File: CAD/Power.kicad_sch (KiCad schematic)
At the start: 84 parts, among them U10 AOZ1284, U18 AP7330-W5-7, U24 LM70860RRXR, U4 AP7361C-33E-13

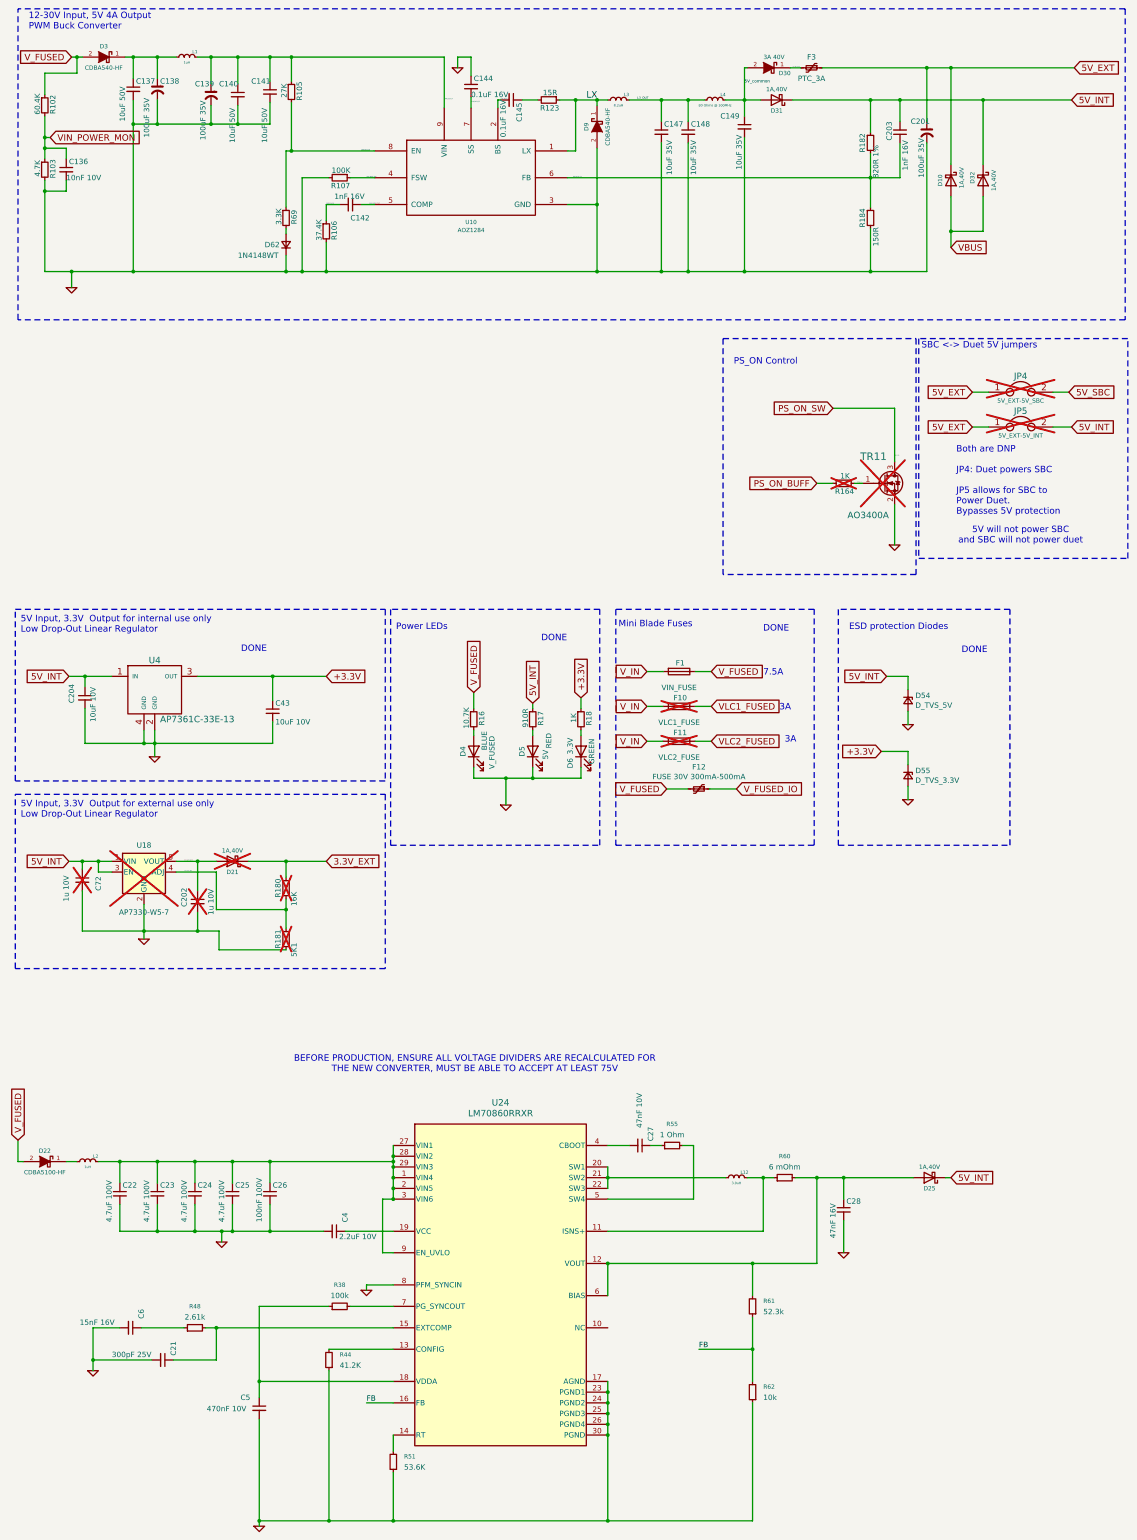
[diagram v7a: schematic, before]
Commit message: Schematic 90%
Still need VIN_POWER_MON and the voltage divider for it, I need to ask robert what voltages are input through there
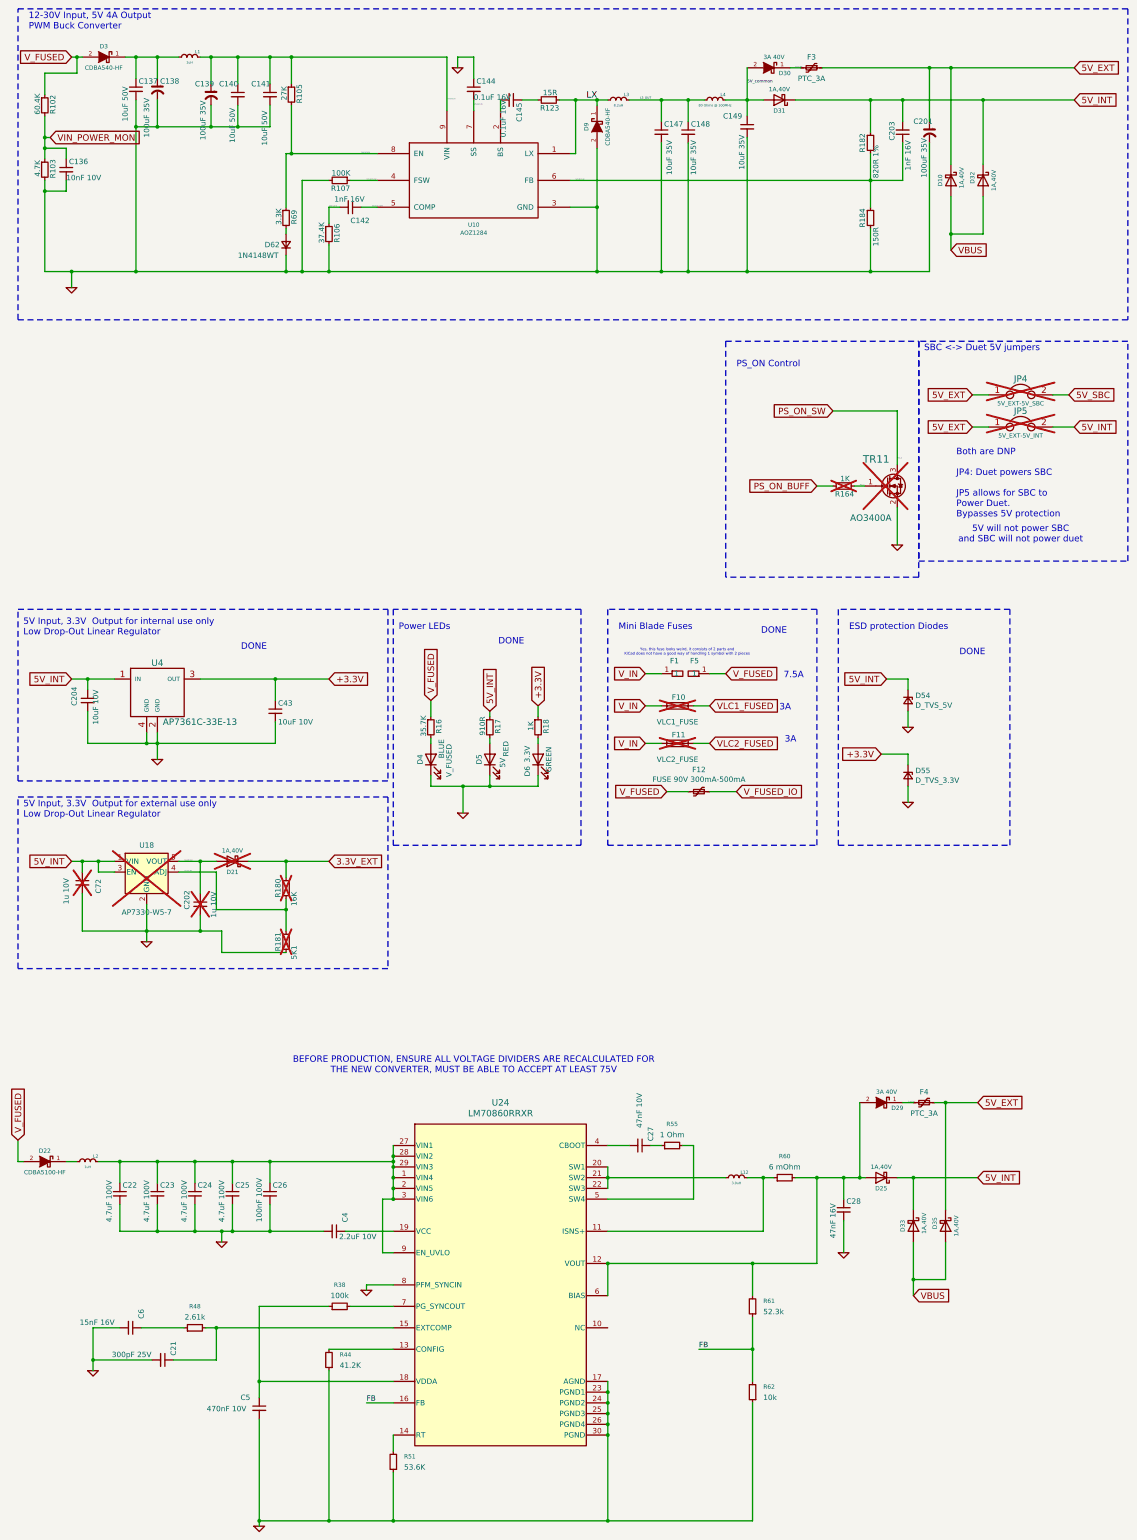
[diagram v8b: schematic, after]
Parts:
- removed F1: VIN_FUSE, Fuse:FuseHolder_Blade_ATO_Littelfuse_FLR_178.6165, symbol Device:Fuse
- added D29: 3A 40V, Diode_SMD:D_SMA, symbol Duet3:CDBA540
- added D33, D35: 1A,40V, Diode_SMD:D_SOD-123F, symbol Device:D_Schottky
- added F1, F5: ~, 3DPotter:01220088Z, symbol 3DPotter:6.35mm_Dia-Ceramic-Fuse-Holder1/2
- added F4: PTC_3A, Fuse:Fuse_1812_4532Metric, symbol Device:Polyfuse_Small
- F12: value FUSE 30V 300mA-500mA -> FUSE 90V 300mA-500mA; footprint Fuse:Fuse_BelFuse_OZCG_1812 -> Fuse:Fuse_1210_3225Metric; LCSC C910832 -> C19723489; Part Number BSMD1812-030-30V -> 1210L010/90AR
- R16: value 10.7K -> 35.7K; footprint Resistor_SMD:R_0402_1005Metric -> Resistor_SMD:R_0603_1608Metric; LCSC C226748 -> C144666; Part Number AC0402FR-0710K7L -> AC0603FR-0735K7L; Rating 50V, 62.5mW -> 75V, 100mW
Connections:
- net 5V_EXT: now also D35.1 (K), F4.1
- net 5V_INT: now also D33.1 (K)
- net 5v_ext_fuse: now also D29.1 (K), F4.2
- net VBUS: now also D33.2 (A), D35.2 (A)
- net V_FUSED: now also F5.1
- net V_IN: now also F1.1
- net at C28.1, D25.2 (A), R60.2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: now also D29.2 (A)
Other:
- note added: "Yes, this fuse looks weird, it consists of 2 parts and KiCad does not have a good way of handling 1 symbol with 2 pieces"
- moved on the sheet: C137, C141, C142, C144, C149, C201, C202, C203, C204, C43, C72, D25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
